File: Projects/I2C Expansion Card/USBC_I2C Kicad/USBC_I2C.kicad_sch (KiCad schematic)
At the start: 17 parts, among them SW1 SW_DIP_x04, U1 MCP2221AxSL

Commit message: Adding new idea and removing R2 from schematic
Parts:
- removed R2: Resistors TBD, R_1206_3216Metric, symbol Device:R_US
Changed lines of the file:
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@@
 		(color 0 0 0 0)
 	)
-	(junction
-		(at 87.63 55.88)
-		(diameter 0)
-		(color 0 0 0 0)
-	)
 	(wire
 		(pts
@@
 	(wire
 		(pts
-			(xy 77.47 55.88) (xy 74.93 55.88)
-		)
-		(stroke
-			(width 0)
-			(type default)
-		)
-	)
-	(wire
-		(pts
 			(xy 166.37 39.37) (xy 163.83 39.37)
 		)
@@
 	(wire
 		(pts
-			(xy 87.63 55.88) (xy 87.63 57.15)
-		)
-		(stroke
-			(width 0)
-			(type default)
-		)
-	)
-	(wire
-		(pts
 			(xy 119.38 29.21) (xy 119.38 27.94)
 		)
@@
 	(wire
 		(pts
-			(xy 87.63 53.34) (xy 87.63 55.88)
+			(xy 87.63 53.34) (xy 87.63 57.15)
 		)
 		(stroke
@@
 		(pts
 			(xy 162.56 71.12) (xy 181.61 71.12)
-		)
-		(stroke
-			(width 0)
-			(type default)
-		)
-	)
-	(wire
-		(pts
-			(xy 85.09 55.88) (xy 87.63 55.88)
 		)
 		(stroke
@@
 					(unit 1)
 				)
-			)
-		)
-	)
-	(symbol
-		(lib_id "Device:R_US")
-		(at 81.28 55.88 90)
-		(unit 1)
-		(exclude_from_sim no)
-		(in_bom yes)
-		(on_board yes)
-		(dnp no)
-		(property "Reference" "R2"
-			(at 84.836 54.61 90)
-			(effects
-				(font
-					(size 1.27 1.27)
-				)
-			)
-		)
-		(property "Value" "Resistors TBD"
-			(at 85.09 70.104 90)
-			(effects
-				(font
-					(size 1.27 1.27)
-				)
-				(hide yes)
-			)
-		)
-		(property "Footprint" "R_1206_3216Metric"
-			(at 81.534 54.864 90)
-			(effects
-				(font
-					(size 1.27 1.27)
-				)
-				(hide yes)
-			)
-		)
-		(property "Datasheet" "~"
-			(at 81.28 55.88 0)
-			(effects
-				(font
-					(size 1.27 1.27)
-				)
-				(hide yes)
-			)
-		)
-		(property "Description" "Resistor, US symbol"
-			(at 81.28 55.88 0)
-			(effects
-				(font
-					(size 1.27 1.27)
-				)
-				(hide yes)
-			)
-		)
-		(pin "1"
-		)
-		(pin "2"
-		)
-		(instances
-			(project "USBC_I2C"
-				(path "/95c30658-c235-4432-9e4a-c0895948e60c"
-					(reference "R2")
-					(unit 1)
-				)

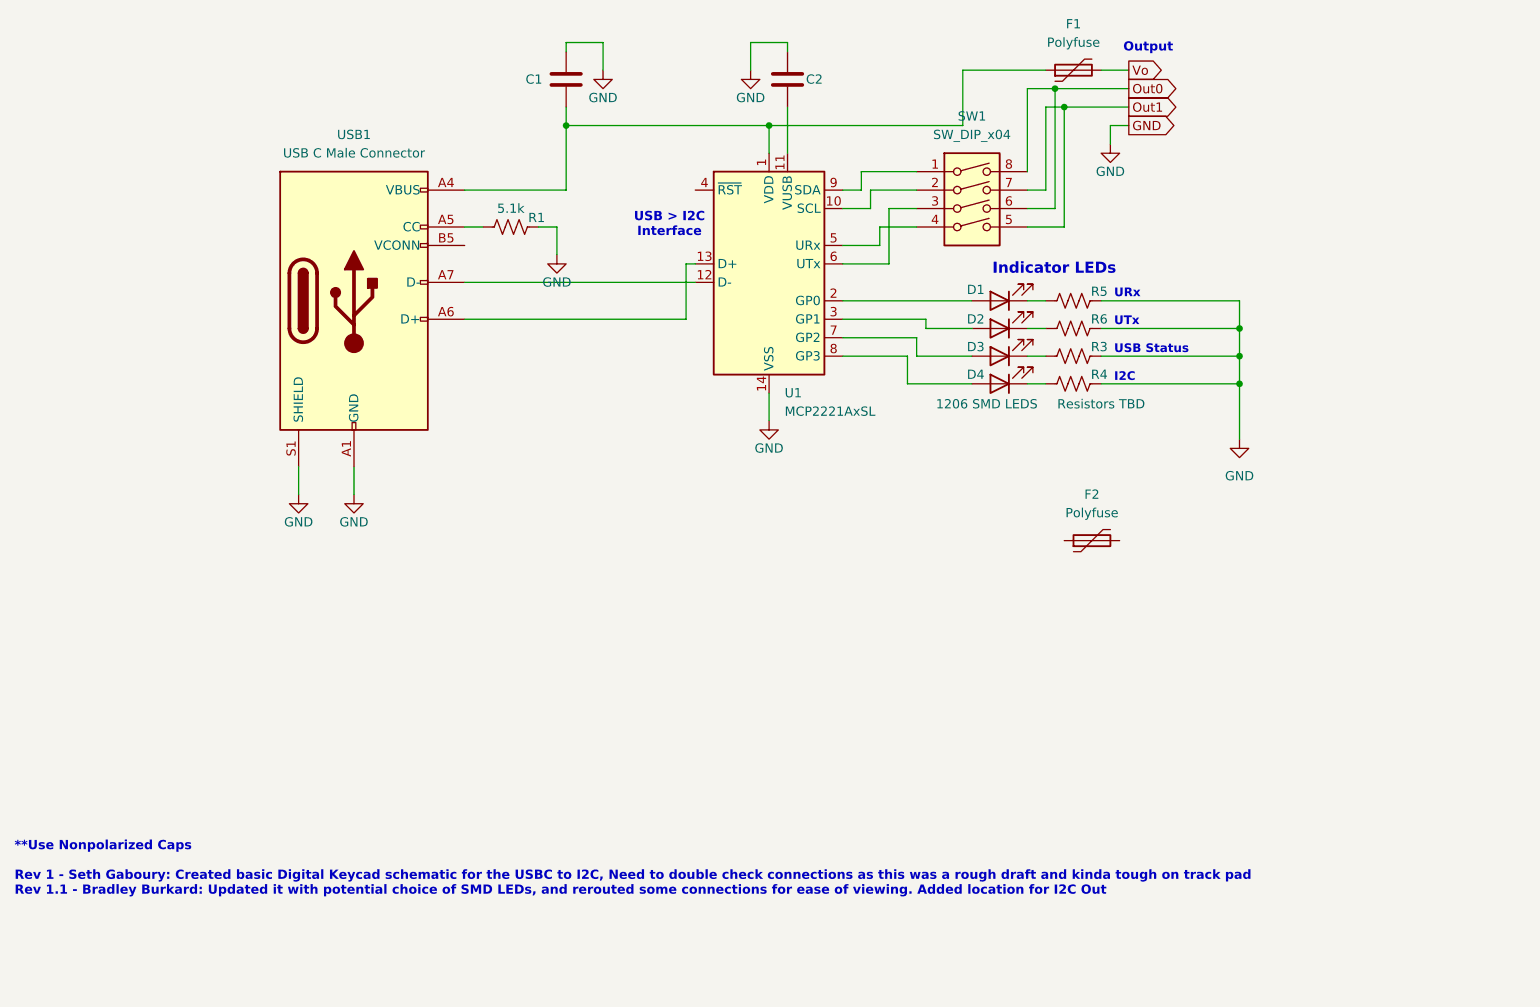
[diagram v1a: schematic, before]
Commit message: Update schematic with OV protection
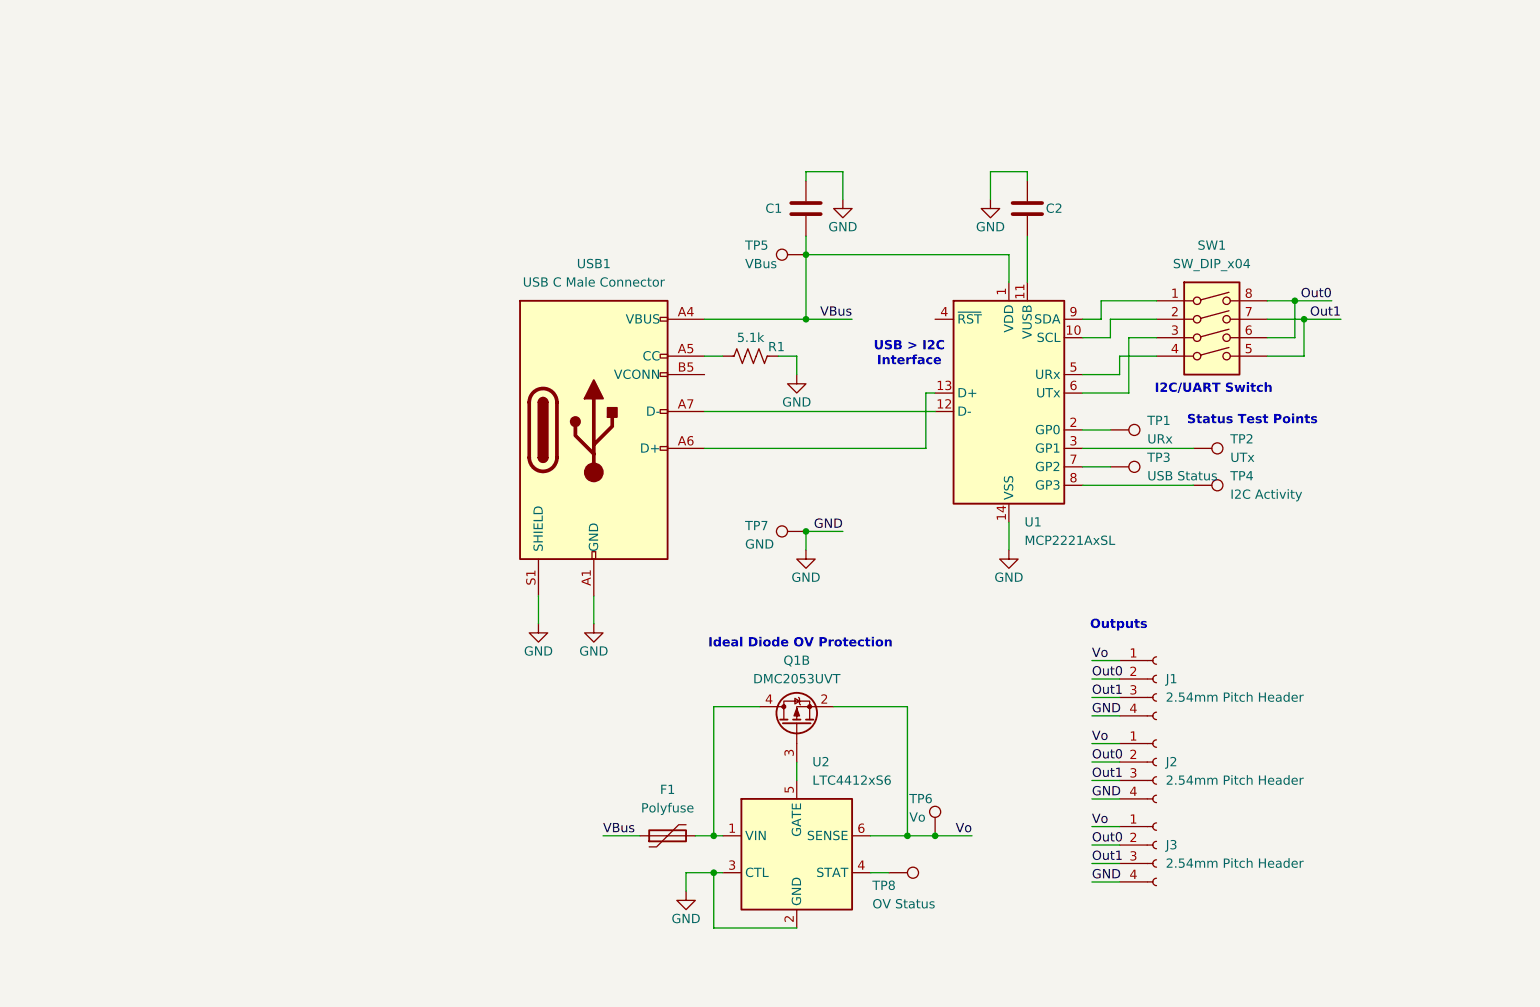
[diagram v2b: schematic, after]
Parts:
- removed D1: 1206 SMD LEDS, LED_SMD:LED_1206_3216Metric, symbol LED:IR26-21C_L110_TR8
- removed D2, D3, D4: IR26-21C_L110_TR8, LED_SMD:LED_1206_3216Metric, symbol LED:IR26-21C_L110_TR8
- removed F2: Polyfuse, symbol Device:Polyfuse
- removed R3, R4, R6: R_US, symbol Device:R_US
- removed R5: Resistors TBD, symbol Device:R_US
- added J1, J2, J3: 2.54mm Pitch Header, PinHeader_1x04_P2.54mm_Vertical, symbol Connector:Conn_01x04_Socket
- added Q1: DMC2053UVT, Package_TO_SOT_SMD:TSOT-23-6, symbol Transistor_FET:DMC2053UVT
- added TP1: URx, symbol Connector:TestPoint
- added TP2: UTx, symbol Connector:TestPoint
- added TP3: USB Status, symbol Connector:TestPoint
- added TP4: I2C Activity, symbol Connector:TestPoint
- added TP5: VBus, symbol Connector:TestPoint
- added TP6: Vo, symbol Connector:TestPoint
- added TP7: GND, symbol Connector:TestPoint
- added TP8: OV Status, symbol Connector:TestPoint
- added U2: LTC4412xS6, Package_TO_SOT_SMD:TSOT-23-6, symbol Power_Management:LTC4412xS6
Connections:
- net GND: now also J1.4 (Pin_4), J2.4 (Pin_4), J3.4 (Pin_4), TP7.1, U2.2 (GND), U2.3 (CTL)
- net Out0: now also J1.2 (Pin_2), J2.2 (Pin_2), J3.2 (Pin_2)
- net Out1: now also J1.3 (Pin_3), J2.3 (Pin_3), J3.3 (Pin_3)
- net Vo: now also J1.1 (Pin_1), J2.1 (Pin_1), J3.1 (Pin_1), Q1.2 (S), TP6.1, U2.6 (SENSE); no longer F1.2
- net VBus: now reaches C1.2, F1.1, U1.1 (VDD), USB1.A4 (VBUS), USB1.A9 (VBUS), USB1.B4 (VBUS), USB1.B9 (VBUS)
- net VBus: now also TP5.1
- net at U1.3 (GP1): now also TP2.1
- net at U1.7 (GP2): now also TP3.1
- net at U1.2 (GP0): now also TP1.1
- net at U1.8 (GP3): now also TP4.1
- new net: Q1.3 (G), U2.5 (GATE)
- new net: F1.2, Q1.4 (D), U2.1 (VIN)
- new net: TP8.1, U2.4 (STAT)
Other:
- note added: "I2C/UART Switch"
- note added: "Ideal Diode OV Protection"
- note added: "Outputs"
- note added: "Status Test Points"
- note removed: "**Use Nonpolarized Caps Rev 1 - Seth Gaboury: Created basic Digital Keycad schematic for the USBC to I2C, Need to double check connections as this was a rough draft and kinda tough on track pad Rev 1.1 - Bradley Burkard: Updated it with potential choice of SMD LEDs, and rerouted some connections for ease of viewing. Added location for I2C Out"
- note removed: "Indicator LEDs"
- note removed: "Output"
- note removed: "URx UTx USB Status I2C"
- moved on the sheet: C1, C2, F1, R1, SW1, U1, USB1

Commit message: Add OV protection to I2C Card
Also includes changing the length of the board, adding a second power plane (Vo), and moving a couple traces slightly to accomodate all these changes.
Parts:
- added R2: 470k, R_1206_3216Metric, symbol Device:R_US
- added TP10: D-, TestPoint_Pad_D1.0mm, symbol Connector:TestPoint
- added TP9: D+, TestPoint_Pad_D1.0mm, symbol Connector:TestPoint
- J2, J3: footprint PinHeader_1x04_P2.54mm_Vertical -> PinHeader_1x04_P2.54mm_Horizontal
- TP1, TP2, TP3, TP4, TP5, TP6, TP7, TP8: footprint (none) -> TestPoint_Pad_D1.0mm
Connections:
- net Out0: no longer SW1.6, SW1.8
- net Out1: no longer SW1.5, SW1.7
- net at U1.13 (D+), USB1.A6 (D+): now also TP9.1
- net at U1.12 (D-), USB1.A7 (D-): now also TP10.1
- net at F1.2, Q1.4 (D), U2.1 (VIN): now also R2.1
- net at TP8.1, U2.4 (STAT): now also R2.2
- new net SCL/UTx: SW1.5, SW1.7
- new net SDA/URx: SW1.6, SW1.8
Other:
- moved on the sheet: F1, TP8

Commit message: Finished improving I2C/UART Card
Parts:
- removed TP10: D-, TestPoint_Pad_D1.0mm, symbol Connector:TestPoint
- removed TP9: D+, TestPoint_Pad_D1.0mm, symbol Connector:TestPoint
- added C3: 10uF, C_1206_3216Metric_Pad1.33x1.80mm_HandSolder, symbol Device:C
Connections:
- net SCL/UTx is gone; now on net Out1: SW1.5, SW1.7
- net SDA/URx is gone; now on net Out0: SW1.6, SW1.8
- net GND: now also C3.2
- net Vo: now also C3.1
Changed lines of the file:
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@@
 	)
 	(junction
-		(at 138.43 83.82)
-		(diameter 0)
-		(color 0 0 0 0)
-	)
-	(junction
 		(at 190.5 66.04)
 		(diameter 0)
@@
 	)
 	(junction
-		(at 127 78.74)
-		(diameter 0)
-		(color 0 0 0 0)
-	)
-	(junction
 		(at 109.22 142.24)
 		(diameter 0)
@@
 	(wire
 		(pts
-			(xy 127 78.74) (xy 139.7 78.74)
+			(xy 107.95 78.74) (xy 139.7 78.74)
 		)
 		(stroke
@@
 	(wire
 		(pts
+			(xy 152.4 144.78) (xy 152.4 148.59)
+		)
+		(stroke
+			(width 0)
+			(type default)
+		)
+	)
+	(wire
+		(pts
 			(xy 163.83 68.58) (xy 163.83 66.04)
 		)
@@
 	(wire
 		(pts
-			(xy 107.95 78.74) (xy 127 78.74)
-		)
-		(stroke
-			(width 0)
-			(type default)
-		)
-	)
-	(wire
-		(pts
 			(xy 121.92 46.99) (xy 121.92 45.72)
 		)
@@
 	(wire
 		(pts
-			(xy 139.7 137.16) (xy 144.78 137.16)
+			(xy 139.7 137.16) (xy 152.4 137.16)
 		)
 		(stroke
@@
 		)
 	)
-	(label "SCL{slash}UTx"
-		(at 199.39 66.04 180)
-		(effects
-			(font
-				(size 1.27 1.27)
-			)
-			(justify right bottom)
-		)
-	)
 	(label "VBus"
 		(at 85.09 137.16 0)
@@
 		)
 	)
-	(label "SDA{slash}URx"
-		(at 198.12 63.5 180)
+	(label "Out1"
+		(at 190.5 66.04 0)
 		(effects
 			(font
 				(size 1.27 1.27)
 			)
-			(justify right bottom)
+			(justify left bottom)
+		)
+	)
+	(label "Out0"
+		(at 189.23 63.5 0)
+		(effects
+			(font
+				(size 1.27 1.27)
+			)
+			(justify left bottom)
 		)
 	)
@@
 	)
 	(symbol
-		(lib_id "Device:Polyfuse")
-		(at 93.98 137.16 90)
+		(lib_id "Device:C")
+		(at 152.4 140.97 0)
 		(unit 1)
 		(exclude_from_sim no)
@@
 		(on_board yes)
 		(dnp no)
-		(fields_autoplaced yes)
-		(property "Reference" "F1"
-			(at 93.98 130.81 90)
+		(property "Reference" "C3"
+			(at 154.94 140.97 0)
 			(effects
 				(font
 					(size 1.27 1.27)
 				)
+				(justify left)
 			)
 		)
-		(property "Value" "Polyfuse"
-			(at 93.98 133.35 90)
+		(property "Value" "10uF"
+			(at 156.21 142.2399 0)
 			(effects
 				(font
 					(size 1.27 1.27)
 				)
+				(justify left)
+				(hide yes)
 			)
 		)
-		(property "Footprint" "Fuse_1206_3216Metric"
-			(at 99.06 135.89 0)
+		(property "Footprint" "C_1206_3216Metric_Pad1.33x1.80mm_HandSolder"
+			(at 153.3652 144.78 0)
 			(effects
 				(font
 					(size 1.27 1.27)
 				)
-				(justify left)
 				(hide yes)
 			)
 		)
 		(property "Datasheet" "~"
-			(at 93.98 137.16 0)
+			(at 152.4 140.97 0)
 			(effects
 				(font
@@
 			)
 		)
-		(property "Description" "Resettable fuse, polymeric positive temperature coefficient"
-			(at 93.98 137.16 0)
+		(property "Description" "Unpolarized capacitor"
+			(at 152.4 140.97 0)
 			(effects
 				(font
@@
 			(project "USBC_I2C"
 				(path "/95c30658-c235-4432-9e4a-c0895948e60c"
-					(reference "F1")
+					(reference "C3")
 					(unit 1)
 				)
@@
 	)
 	(symbol
-		(lib_id "Connector:TestPoint")
-		(at 163.83 86.36 270)
+		(lib_id "Device:Polyfuse")
+		(at 93.98 137.16 90)
 		(unit 1)
 		(exclude_from_sim no)
@@
 		(dnp no)
 		(fields_autoplaced yes)
-		(property "Reference" "TP3"
-			(at 168.91 85.0899 90)
+		(property "Reference" "F1"
+			(at 93.98 130.81 90)
 			(effects
 				(font
 					(size 1.27 1.27)
 				)
-				(justify left)
 			)
 		)
-		(property "Value" "USB Status"
-			(at 168.91 87.6299 90)
+		(property "Value" "Polyfuse"
+			(at 93.98 133.35 90)
 			(effects
 				(font
 					(size 1.27 1.27)
 				)
-				(justify left)
 			)
 		)
-		(property "Footprint" "TestPoint_Pad_D1.0mm"
-			(at 163.83 91.44 0)
+		(property "Footprint" "Fuse_1206_3216Metric"
+			(at 99.06 135.89 0)
 			(effects
 				(font
 					(size 1.27 1.27)
 				)
+				(justify left)
 				(hide yes)
 			)
 		)
 		(property "Datasheet" "~"
-			(at 163.83 91.44 0)
+			(at 93.98 137.16 0)
 			(effects
 				(font
@@
 			)
 		)
-		(property "Description" "test point"
-			(at 163.83 86.36 0)
+		(property "Description" "Resettable fuse, polymeric positive temperature coefficient"
+			(at 93.98 137.16 0)
 			(effects
 				(font
@@
 			)
 		)
+		(pin "2"
+		)
 		(pin "1"
 		)
@@
 			(project "USBC_I2C"
 				(path "/95c30658-c235-4432-9e4a-c0895948e60c"
-					(reference "TP3")
+					(reference "F1")
 					(unit 1)
 				)
@@
 	(symbol
 		(lib_id "Connector:TestPoint")
-		(at 138.43 83.82 180)
+		(at 163.83 86.36 270)
 		(unit 1)
 		(exclude_from_sim no)
@@
 		(on_board yes)
 		(dnp no)
-		(property "Reference" "TP9"
-			(at 140.462 91.694 0)
+		(fields_autoplaced yes)
+		(property "Reference" "TP3"
+			(at 168.91 85.0899 90)
 			(effects
 				(font
@@
 			)
 		)
-		(property "Value" "D+"
-			(at 140.462 89.154 0)
+		(property "Value" "USB Status"
+			(at 168.91 87.6299 90)
 			(effects
 				(font
@@
 		)
 		(property "Footprint" "TestPoint_Pad_D1.0mm"
-			(at 133.35 83.82 0)
+			(at 163.83 91.44 0)
 			(effects
 				(font
@@
 		)
 		(property "Datasheet" "~"
-			(at 133.35 83.82 0)
+			(at 163.83 91.44 0)
 			(effects
 				(font
@@
 		)
 		(property "Description" "test point"
-			(at 138.43 83.82 0)
+			(at 163.83 86.36 0)
 			(effects
 				(font
@@
 			(project "USBC_I2C"
 				(path "/95c30658-c235-4432-9e4a-c0895948e60c"
-					(reference "TP9")
+					(reference "TP3")
 					(unit 1)
 				)
@@
 	)
 	(symbol
-		(lib_id "Connector:TestPoint")
-		(at 121.92 95.25 90)
+		(lib_id "power:GND")
+		(at 152.4 148.59 0)
 		(unit 1)
 		(exclude_from_sim no)
@@
 		(on_board yes)
 		(dnp no)
-		(property "Reference" "TP7"
-			(at 113.538 94.488 90)
+		(property "Reference" "#PWR02"
+			(at 152.4 154.94 0)
 			(effects
 				(font
 					(size 1.27 1.27)
 				)
-				(justify right)
+				(hide yes)
 			)
 		)
 		(property "Value" "GND"
-			(at 113.538 97.028 90)
+			(at 152.4 152.4 0)
 			(effects
 				(font
 					(size 1.27 1.27)
 				)
-				(justify right)
 			)
 		)
-		(property "Footprint" "TestPoint_Pad_D1.0mm"
-			(at 121.92 90.17 0)
+		(property "Footprint" ""
+			(at 152.4 148.59 0)
 			(effects
 				(font
@@
 			)
 		)
-		(property "Datasheet" "~"
-			(at 121.92 90.17 0)
+		(property "Datasheet" ""
+			(at 152.4 148.59 0)
 			(effects
 				(font
@@
 			)
 		)
-		(property "Description" "test point"
-			(at 121.92 95.25 0)
+		(property "Description" "Power symbol creates a global label with name \"GND\" , ground"
+			(at 152.4 148.59 0)
 			(effects
 				(font
@@
 			(project "USBC_I2C"
 				(path "/95c30658-c235-4432-9e4a-c0895948e60c"
-					(reference "TP7")
+					(reference "#PWR02")
 					(unit 1)
 				)
@@
 	(symbol
 		(lib_id "Connector:TestPoint")
-		(at 139.7 137.16 0)
+		(at 121.92 95.25 90)
 		(unit 1)
 		(exclude_from_sim no)
@@
 		(on_board yes)
 		(dnp no)
-		(property "Reference" "TP6"
-			(at 136.144 132.08 0)
+		(property "Reference" "TP7"
+			(at 113.538 94.488 90)
 			(effects
 				(font
 					(size 1.27 1.27)
 				)
-				(justify left)
+				(justify right)
 			)
 		)
-		(property "Value" "Vo"
-			(at 136.144 134.62 0)
+		(property "Value" "GND"
+			(at 113.538 97.028 90)
 			(effects
 				(font
 					(size 1.27 1.27)
 				)
-				(justify left)
+				(justify right)
 			)
 		)
 		(property "Footprint" "TestPoint_Pad_D1.0mm"
-			(at 144.78 137.16 0)
+			(at 121.92 90.17 0)
 			(effects
 				(font
@@
 		)
 		(property "Datasheet" "~"
-			(at 144.78 137.16 0)
+			(at 121.92 90.17 0)
 			(effects
 				(font
@@
 		)
 		(property "Description" "test point"
-			(at 139.7 137.16 0)
+			(at 121.92 95.25 0)
 			(effects
 				(font
@@
 			(project "USBC_I2C"
 				(path "/95c30658-c235-4432-9e4a-c0895948e60c"
-					(reference "TP6")
+					(reference "TP7")
 					(unit 1)
 				)
@@
 	(symbol
 		(lib_id "Connector:TestPoint")
-		(at 127 78.74 0)
+		(at 139.7 137.16 0)
 		(unit 1)
 		(exclude_from_sim no)
@@
 		(on_board yes)
 		(dnp no)
-		(property "Reference" "TP10"
-			(at 124.968 71.12 0)
+		(property "Reference" "TP6"
+			(at 136.144 132.08 0)
 			(effects
 				(font
@@
 			)
 		)
-		(property "Value" "D-"
-			(at 124.968 73.66 0)
+		(property "Value" "Vo"
+			(at 136.144 134.62 0)
 			(effects
 				(font
@@
 		)
 		(property "Footprint" "TestPoint_Pad_D1.0mm"
-			(at 132.08 78.74 0)
+			(at 144.78 137.16 0)
 			(effects
 				(font
@@
 		)
 		(property "Datasheet" "~"
-			(at 132.08 78.74 0)
+			(at 144.78 137.16 0)
 			(effects
 				(font
@@
 		)
 		(property "Description" "test point"
-			(at 127 78.74 0)
+			(at 139.7 137.16 0)
 			(effects
 				(font
@@
 			(project "USBC_I2C"
 				(path "/95c30658-c235-4432-9e4a-c0895948e60c"
-					(reference "TP10")
+					(reference "TP6")
 					(unit 1)
 				)
